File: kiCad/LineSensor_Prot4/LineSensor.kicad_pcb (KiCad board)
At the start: 2 copper layers, 100 x 100 mm, 109 parts, among them J1 Conn_01x04_Socket, J2 Conn_01x02_Socket, Q1 Q_Photo_NPN, Q10 Q_Photo_NPN, Q11 Q_Photo_NPN, Q12 Q_Photo_NPN, Q13 Q_Photo_NPN, Q14 Q_Photo_NPN, Q15 Q_Photo_NPN, Q16 Q_Photo_NPN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

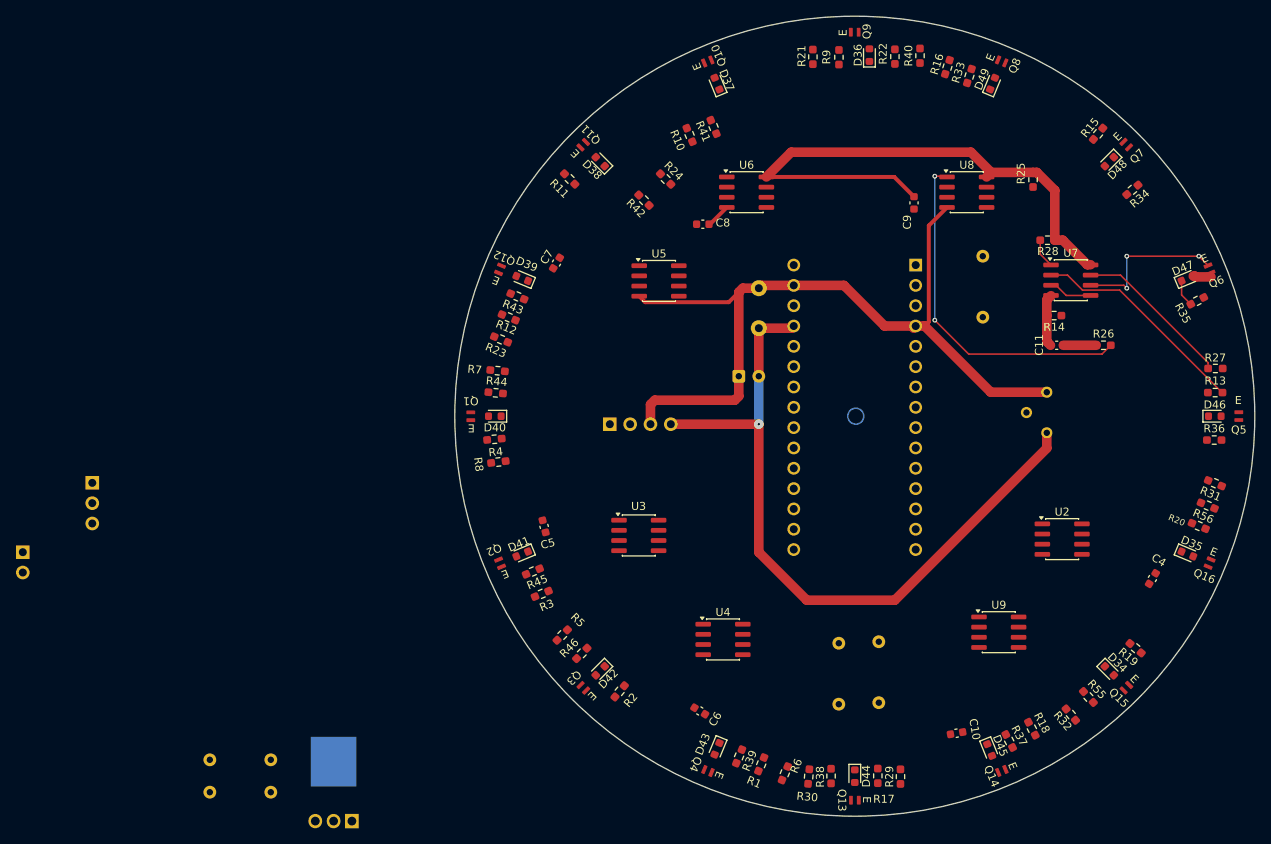
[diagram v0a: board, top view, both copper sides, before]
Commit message: prot4のdrc警告なし
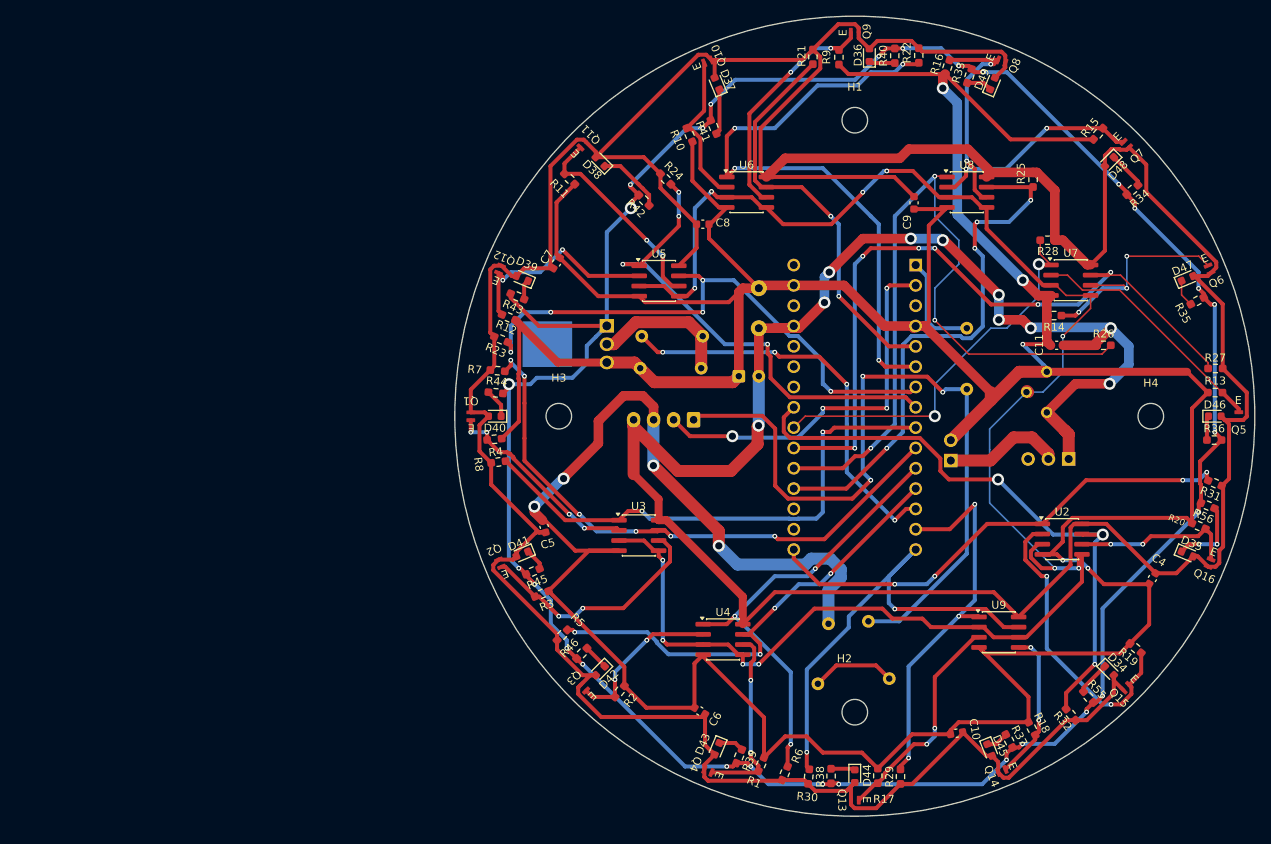
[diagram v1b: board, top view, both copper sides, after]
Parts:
- added H1: MountingHole, MountingHole:MountingHole_3.2mm_M3, F.Cu at (150.0, 63.0)
- added H2: MountingHole, MountingHole:MountingHole_3.2mm_M3, F.Cu at (150.0, 137.0)
- added H3: MountingHole, MountingHole:MountingHole_3.2mm_M3, F.Cu at (113.0, 100.0)
- added H4: MountingHole, MountingHole:MountingHole_3.2mm_M3, F.Cu at (187.0, 100.0)
- J1: footprint Connector_PinSocket_2.54mm:PinSocket_1x04_P2.54mm_Vertical -> Connector_JST:JST_XH_B4B-XH-A_1x04_P2.50mm_Vertical
- moved SW2 122.1 mm to (176.7, 105.3), turned to 90 degrees
- moved J2 116.6 mm to (162.0, 105.5), turned to 0 degrees
- moved R84 70.4 mm to (123.4, 90.0), turned to 0 degrees
- moved R85 70.3 mm to (123.2, 94.0), turned to 0 degrees
- moved Q17 69.6 mm to (119.0, 88.7), turned to -90 degrees
- moved J1 10.5 mm to (129.8, 100.5), turned to 180 degrees
- moved R49 9.22 mm to (164.0, 96.6)
- moved R50 3.65 mm to (145.4, 133.4), turned to 80 degrees
- moved R40 3.15 mm to (155.0, 54.9)
- moved R22 2.99 mm to (158.0, 54.9)
- moved R51 2.86 mm to (151.7, 125.6), turned to -70 degrees
- moved RV1 2.55 mm to (174.0, 97.0)
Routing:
- net VCC: track 169.7 -> 701.2 mm, vias 1 -> 10
- net GND: track 112.4 -> 574.5 mm, vias 0 -> 9
- net Net-(Q17-D): track 0.00 -> 320.0 mm, vias 0 -> 27
- net Net-(U2A-+): track 5.48 -> 217.8 mm, vias 0 -> 11
- net Net-(J1-Pin_1): track 0.00 -> 95.5 mm, vias 0 -> 3
- net Net-(A1-D3): track 0.00 -> 77.2 mm, vias 0 -> 4
- net Net-(A1-A4): track 0.00 -> 76.0 mm, vias 0 -> 3
- net Net-(A1-D7): track 0.00 -> 73.6 mm, vias 0 -> 6
- net Net-(A1-D4): track 0.00 -> 71.0 mm, vias 0 -> 5
- net Net-(A1-A2): track 19.9 -> 90.7 mm, vias 0 -> 6
- net Net-(A1-A0): track 0.00 -> 67.7 mm, vias 0 -> 4
- net Net-(A1-D6): track 0.00 -> 65.8 mm, vias 0 -> 2
- net Net-(A1-D5): track 0.00 -> 61.1 mm, vias 0 -> 4
- net Net-(A1-D13): track 0.00 -> 61.0 mm, vias 0 -> 4
- net Net-(A1-D12): track 0.00 -> 58.8 mm, vias 0 -> 2
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
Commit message: 11/19バケモンスケジュール
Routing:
- net Net-(A1-D1/TX): track 12.9 -> 11.2 mm
- net Net-(A1-A1): track 94.2 -> 92.6 mm
- net Net-(A1-A0): track 67.7 -> 66.3 mm
- net GND: track 574.5 -> 573.7 mm
- added copper zone on B.Cu, net GND
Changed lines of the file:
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@@
 	)
 	(segment
-		(start 159.937925 89)
-		(end 159 88.062075)
+		(start 161.249 87.249)
+		(end 161 87)
+		(width 0.5)
+		(layer "B.Cu")
+		(net 7)
+	)
+	(segment
+		(start 163 89)
+		(end 161.751 87.751)
+		(width 0.5)
+		(layer "B.Cu")
+		(net 7)
+	)
+	(segment
+		(start 161 87)
+		(end 161 84.499)
+		(width 0.5)
+		(layer "B.Cu")
+		(net 7)
+	)
+	(segment
+		(start 161.249 87.311075)
+		(end 161.249 87.249)
 		(width 0.5)
 		(layer "B.Cu")
@@
 	(segment
 		(start 164 89)
-		(end 159.937925 89)
+		(end 163 89)
 		(width 0.5)
 		(layer "B.Cu")
@@
 	)
 	(segment
-		(start 159 82.499)
+		(start 161 84.499)
 		(end 157.61 81.109)
 		(width 0.5)
@@
 	)
 	(segment
-		(start 159 88.062075)
-		(end 159 82.499)
+		(start 161.751 87.751)
+		(end 161.688925 87.751)
+		(width 0.5)
+		(layer "B.Cu")
+		(net 7)
+	)
+	(segment
+		(start 161.688925 87.751)
+		(end 161.249 87.311075)
 		(width 0.5)
 		(layer "B.Cu")
@@
 	(segment
 		(start 164.235579 92.235579)
-		(end 160 88)
+		(end 162 90)
+		(width 0.2)
+		(layer "F.Cu")
+		(net 13)
+	)
+	(segment
+		(start 180.898999 92.235579)
+		(end 164.235579 92.235579)
 		(width 0.2)
 		(layer "F.Cu")
@@
 	)
 	(segment
-		(start 180.898999 92.235579)
-		(end 164.235579 92.235579)
-		(width 0.2)
-		(layer "F.Cu")
-		(net 13)
-	)
-	(segment
 		(start 152 104)
 		(end 151 105)
@@
 	)
 	(segment
+		(start 162 90)
+		(end 162 87)
+		(width 0.2)
+		(layer "F.Cu")
+		(net 13)
+	)
+	(segment
 		(start 160 70)
 		(end 161.43 70)
@@
 	)
 	(via
-		(at 160 88)
+		(at 162 87)
 		(size 0.6)
 		(drill 0.3)
@@
 	)
 	(segment
+		(start 160 75)
+		(end 160 70)
+		(width 0.2)
+		(layer "B.Cu")
+		(net 13)
+	)
+	(segment
 		(start 163 78)
 		(end 160 75)
@@
 	)
 	(segment
-		(start 160 88)
-		(end 160 84)
+		(start 163 81)
+		(end 163 78)
 		(width 0.2)
 		(layer "B.Cu")
@@
 	)
 	(segment
-		(start 163 81)
-		(end 163 78)
+		(start 162 87)
+		(end 162 82)
 		(width 0.2)
 		(layer "B.Cu")
@@
 	)
 	(segment
-		(start 160 84)
+		(start 162 82)
 		(end 163 81)
 		(width 0.2)
@@
 	)
 	(segment
-		(start 160 75)
-		(end 160 70)
-		(width 0.2)
-		(layer "B.Cu")
-		(net 13)
-	)
-	(segment
 		(start 155 101)
 		(end 155 75)
@@
 	)
 	(segment
+		(start 157.399155 74.110695)
+		(end 161.319304 74.110695)
+		(width 0.5)
+		(layer "F.Cu")
+		(net 23)
+	)
+	(segment
+		(start 161.524999 73.905)
+		(end 159.249 76.180999)
+		(width 0.5)
+		(layer "F.Cu")
+		(net 23)
+	)
+	(segment
 		(start 108.05 88.458)
 		(end 107.586 87.994)
@@
 	)
 	(segment
+		(start 159.249 88.209)
+		(end 158.729 88.729)
+		(width 0.5)
+		(layer "F.Cu")
+		(net 23)
+	)
+	(segment
 		(start 174.525 84.936)
 		(end 172.936 84.936)
@@
 	)
 	(segment
-		(start 157.399155 74.110695)
-		(end 161.319304 74.110695)
-		(width 0.5)
-		(layer "F.Cu")
-		(net 23)
-	)
-	(segment
 		(start 138 84)
 		(end 139 84)
@@
 	)
 	(segment
-		(start 157.61 88.729)
-		(end 158.729 88.729)
-		(width 1.2)
-		(layer "F.Cu")
-		(net 23)
-	)
-	(segment
 		(start 113.6 107.75)
 		(end 117.95 103.4)
@@
 	)
 	(segment
-		(start 161.963548 139.274826)
-		(end 162.986374 138.252)
+		(start 159.249 76.180999)
+		(end 159.249 88.209)
 		(width 0.5)
 		(layer "F.Cu")
@@
 	)
 	(segment
-		(start 159.249 76.180999)
-		(end 159.249 88.209)
+		(start 161.963548 139.274826)
+		(end 162.986374 138.252)
 		(width 0.5)
 		(layer "F.Cu")
@@
 	)
 	(segment
+		(start 161.319304 74.110695)
+		(end 161.524999 73.905)
+		(width 0.5)
+		(layer "F.Cu")
+		(net 23)
+	)
+	(segment
 		(start 113.115 80.19)
 		(end 117.925001 85.000001)
@@
 	)
 	(segment
+		(start 157 88.729)
+		(end 157.61 88.729)
+		(width 1.2)
+		(layer "F.Cu")
+		(net 23)
+	)
+	(segment
 		(start 116.759 116.81)
 		(end 111.715 121.854)
@@
 	)
 	(segment
-		(start 161.319304 74.110695)
-		(end 161.524999 73.905)
-		(width 0.5)
-		(layer "F.Cu")
-		(net 23)
-	)
-	(segment
 		(start 184.400984 128.413456)
 		(end 183.15844 129.656)
@@
 	(segment
 		(start 153.729 88.729)
-		(end 157.61 88.729)
+		(end 157 88.729)
 		(width 1.2)
 		(layer "F.Cu")
@@
 	)
 	(segment
+		(start 157 88.729)
+		(end 158.729 88.729)
+		(width 1.2)
+		(layer "F.Cu")
+		(net 23)
+	)
+	(segment
 		(start 162 103)
 		(end 167 98)
@@
 	)
 	(segment
-		(start 161.524999 73.905)
-		(end 159.249 76.180999)
-		(width 0.5)
-		(layer "F.Cu")
-		(net 23)
-	)
-	(segment
 		(start 114.4305 124.5695)
 		(end 111.715 121.854)
@@
 		(start 171 91)
 		(end 174.327195 91)
-		(width 0.5)
+		(width 1.2)
 		(layer "F.Cu")
 		(net 23)
@@
 	)
 	(segment
-		(start 157.339 89)
-		(end 157.61 88.729)
-		(width 1.2)
-		(layer "F.Cu")
-		(net 23)
-	)
-	(segment
 		(start 170.55 94.45)
 		(end 174 94.45)
@@
 		(net 23)
 	)
-	(segment
-		(start 159.249 88.209)
-		(end 158.729 88.729)
-		(width 0.5)
-		(layer "F.Cu")
-		(net 23)
-	)
 	(via
 		(at 133 116.2)
@@
 	)
 	(segment
-		(start 173.6 93.6)
-		(end 173.6 94.05)
-		(width 0.5)
-		(layer "B.Cu")
-		(net 23)
-	)
-	(segment
 		(start 144.541318 117.8085)
 		(end 143.8085 118.541318)
@@
 	)
 	(segment
-		(start 174 94)
-		(end 173.6 93.6)
-		(width 0.5)
-		(layer "B.Cu")
-		(net 23)
-	)
-	(segment
 		(start 173.6 93.6)
 		(end 171 91)
-		(width 0.5)
+		(width 1.2)
 		(layer "B.Cu")
 		(net 23)
@@
 	)
 	(segment
+		(start 156.442 92.558)
+		(end 156 93)
+		(width 0.5)
+		(layer "B.Cu")
+		(net 26)
+	)
+	(segment
 		(start 163.481818 90.251)
 		(end 164.518182 90.251)
@@
 	)
 	(segment
-		(start 156 91.071818)
-		(end 157.091818 89.98)
-		(width 0.5)
-		(layer "B.Cu")
-		(net 26)
-	)
-	(segment
 		(start 164.518182 90.251)
 		(end 166 88.769182)
@@
 	)
 	(segment
-		(start 169.277818 75.722182)
-		(end 172 73)
+		(start 163.481818 90.251)
+		(end 161.174818 92.558)
 		(width 0.5)
 		(layer "B.Cu")
@@
 	)
 	(segment
-		(start 156 102)
-		(end 156 91.071818)
+		(start 169.277818 75.722182)
+		(end 172 73)
 		(width 0.5)
 		(layer "B.Cu")
@@
 	)
 	(segment
-		(start 157.091818 89.98)
-		(end 163.210818 89.98)
+		(start 161.174818 92.558)
+		(end 156.442 92.558)
 		(width 0.5)
 		(layer "B.Cu")
@@
 	)
 	(segment
-		(start 165.277818 75.722182)
-		(end 169.277818 75.722182)
+		(start 156 102)
+		(end 156 93)
 		(width 0.5)
 		(layer "B.Cu")
@@
 	)
 	(segment
-		(start 163.210818 89.98)
-		(end 163.481818 90.251)
+		(start 165.277818 75.722182)
+		(end 169.277818 75.722182)
 		(width 0.5)
 		(layer "B.Cu")
@@
 		(net 67)
 	)
+	(zone
+		(net 23)
+		(net_name "GND")
+		(layer "B.Cu")
+		(name "gnd")
+		(hatch edge 0.5)
+		(connect_pads
+			(clearance 0.3)
+		)
+		(min_thickness 0.25)
+		(filled_areas_thickness no)
+		(fill yes
+			(thermal_gap 0.5)
+			(thermal_bridge_width 0.5)
+		)
+		(polygon
+			(pts
+				(xy 146 51) (xy 134 53) (xy 131 54) (xy 129 55) (xy 117 63) (xy 111 69) (xy 104 81) (xy 102 88)
+				(xy 101 98) (xy 101 106) (xy 103 116) (xy 104 119) (xy 107 125) (xy 114 133) (xy 115 135) (xy 118 138)
+				(xy 124 142) (xy 131 146) (xy 144 149) (xy 146 149) (xy 152 150) (xy 155 149) (xy 166 147) (xy 171 145)
+				(xy 183 137) (xy 185 135) (xy 194 123) (xy 197 116) (xy 200 98) (xy 196 81) (xy 186 66) (xy 170 55)
+				(xy 169 54) (xy 152 51) (xy 149 50)
+			)
+		)
+	)
 	(embedded_fonts no)
